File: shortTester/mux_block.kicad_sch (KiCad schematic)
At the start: 8 parts

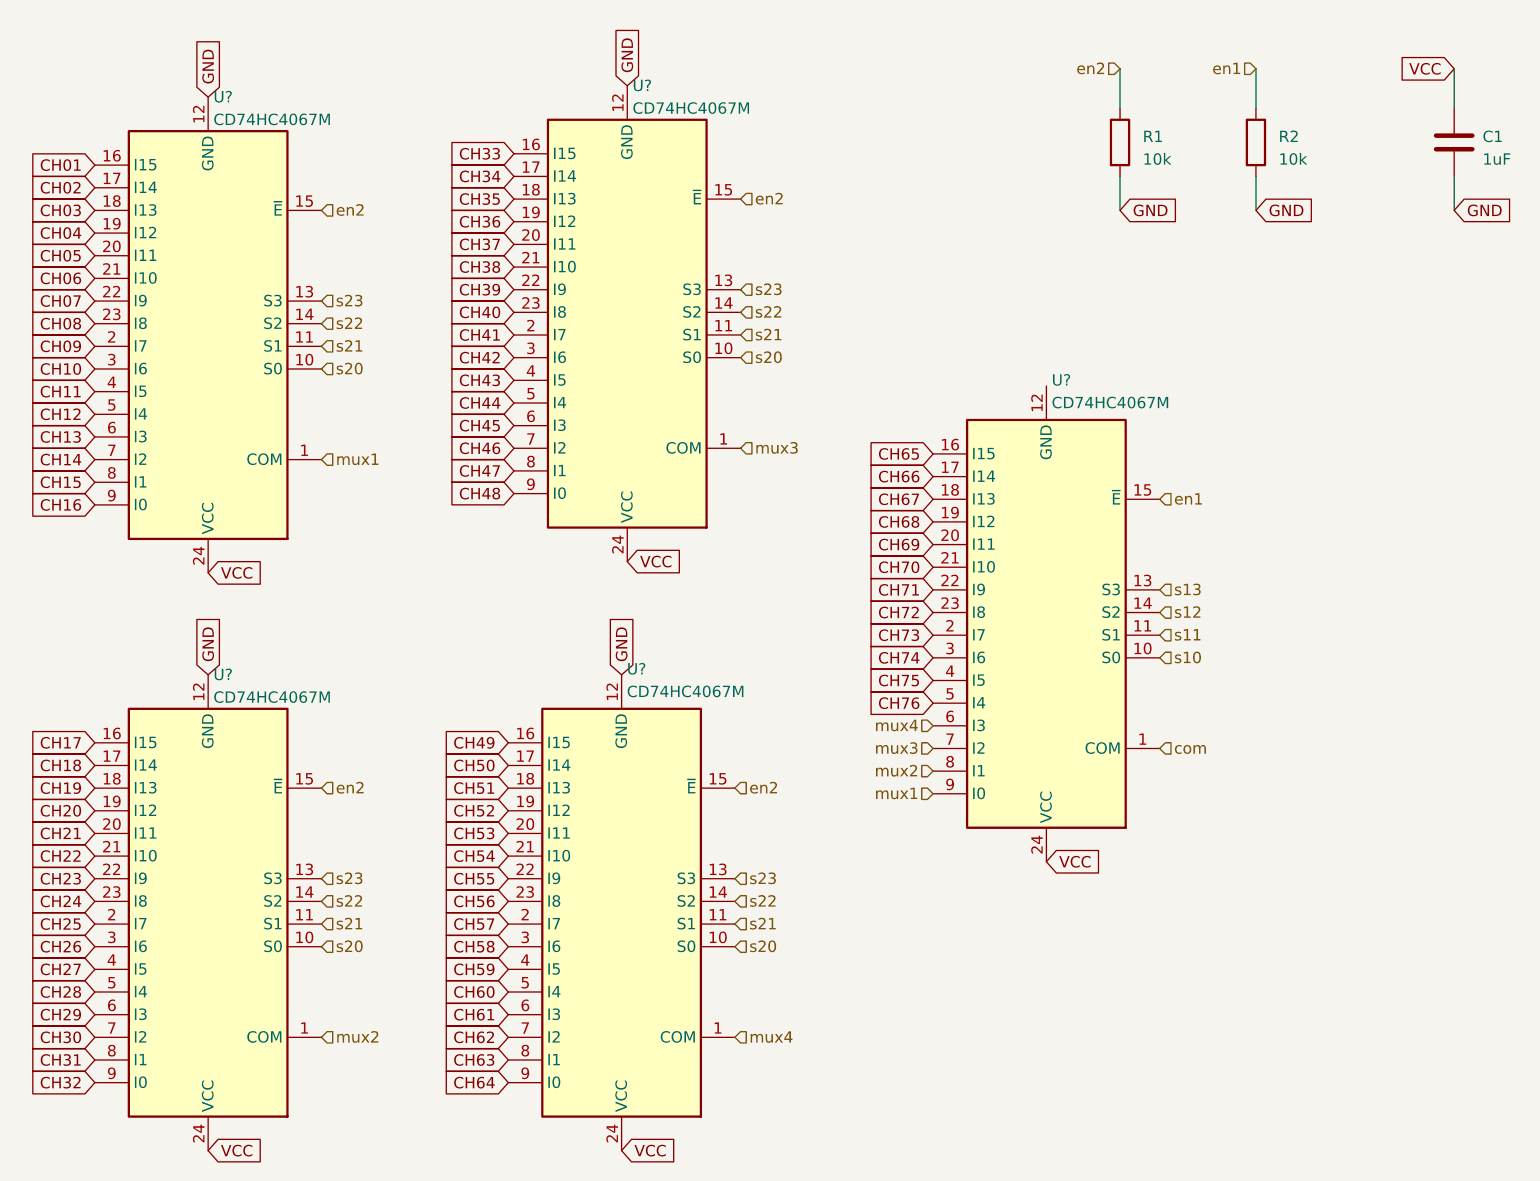
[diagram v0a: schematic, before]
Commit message: Fixed missing tracks. Simplified MUx GND. Added software.
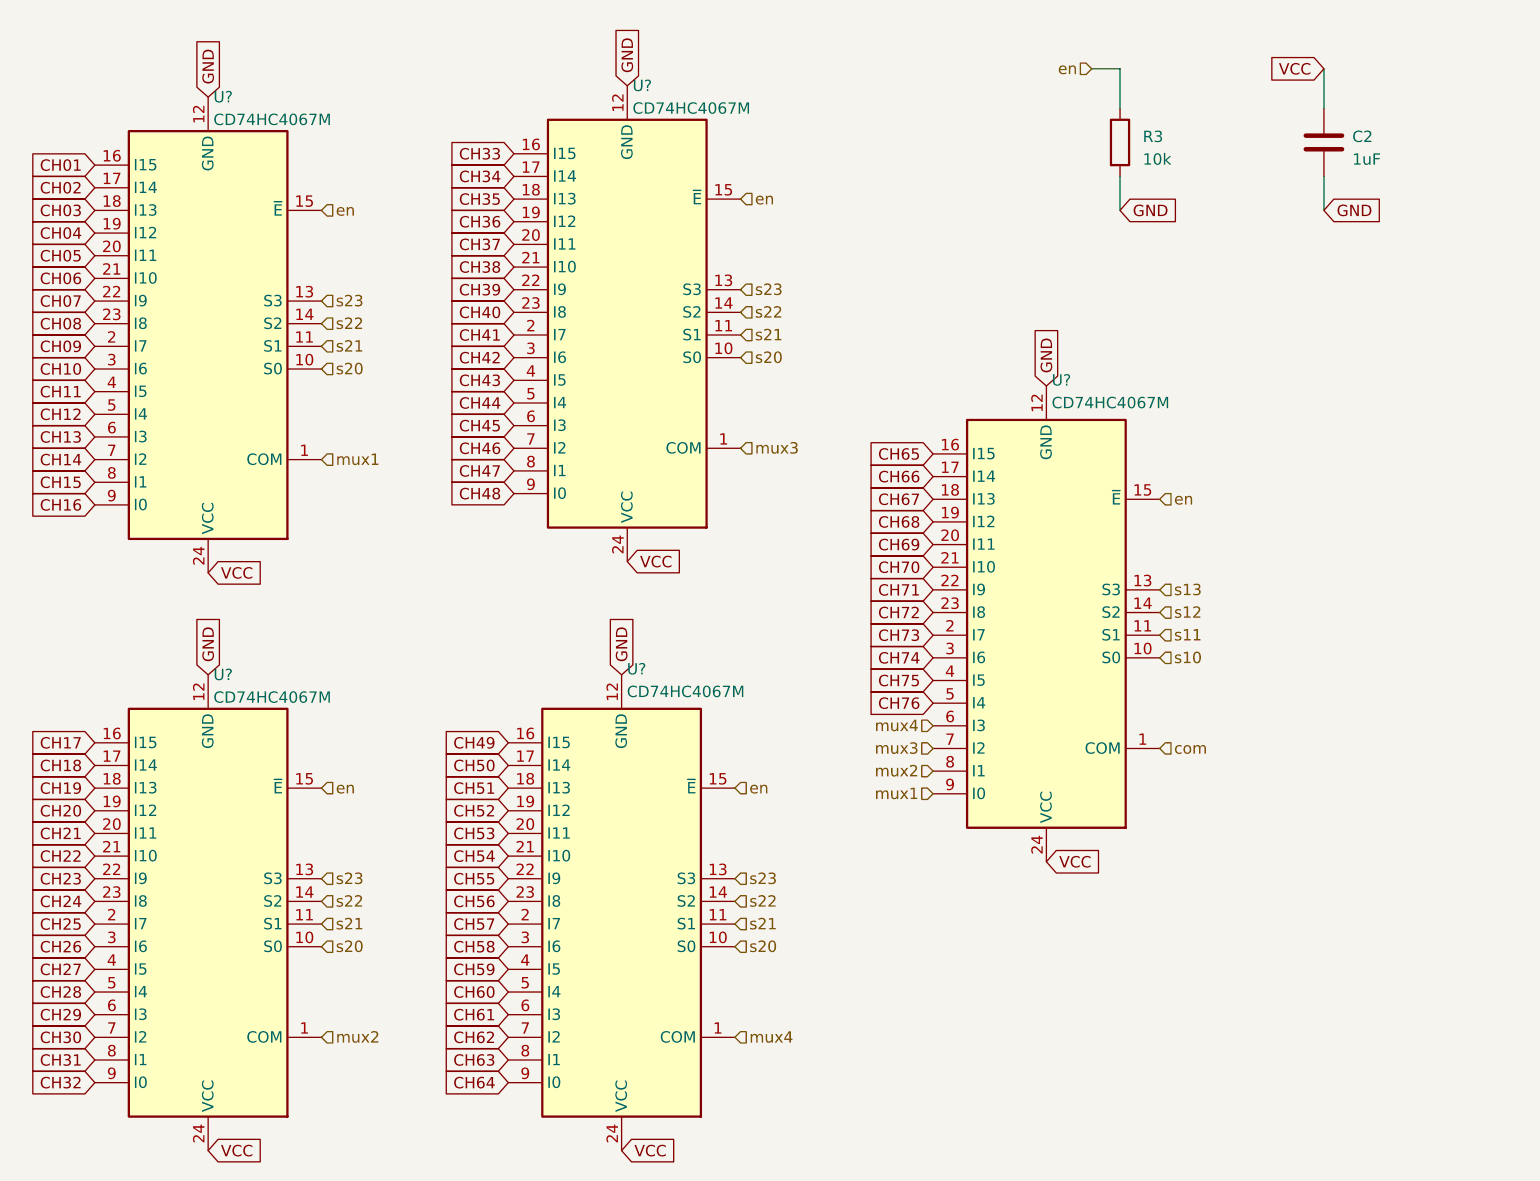
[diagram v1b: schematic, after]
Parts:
- removed R2: 10k, Resistor_SMD:R_1210_3225Metric_Pad1.30x2.65mm_HandSolder, symbol Device:R
- renumbered C1 to C2, R1 to R3
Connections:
- net en2 is gone; now on net en: R3.1, U?.15 (~{E}), U?.15 (~{E}), U?.15 (~{E}), U?.15 (~{E})
- net GND: now also U?.12 (GND)
- net en1 renamed en
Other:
- moved on the sheet: C2
